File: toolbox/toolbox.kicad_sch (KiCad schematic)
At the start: 0 parts

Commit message: added logic shifting
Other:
- removed sheet circuit-proctection
- added sheet logic-shifting (logic-shifting.kicad_sch)
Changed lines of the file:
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@@
 (kicad_sch (version 20211123) (generator eeschema)
   (paper "A4")
-  (sheet (at 45.72 73.66) (size 41.91 20.32) (fields_autoplaced)
+  (sheet (at 46.99 38.1) (size 45.72 17.78) (fields_autoplaced)
     (stroke (width 0.1524) (type solid) (color 0 0 0 0))
     (fill (color 0 0 0 0.0000))
-    (property "Sheet name" "circuit-proctection" (id 0) (at 45.72 72.9484 0)
+    (property "Sheet name" "LED-indicators" (id 0) (at 46.99 37.3884 0)
       (effects (font (size 1.27 1.27)) (justify left bottom))
     )
-    (property "Sheet file" "circuit-proctection.kicad_sch" (id 1) (at 45.72 94.5646 0)
+    (property "Sheet file" "untitled.kicad_sch" (id 1) (at 46.99 56.4646 0)
       (effects (font (size 1.27 1.27)) (justify left top))
     )
   )
-  (sheet (at 39.37 38.1) (size 45.72 17.78) (fields_autoplaced)
+  (sheet (at 46.99 66.04) (size 45.72 17.78) (fields_autoplaced)
     (stroke (width 0.1524) (type solid) (color 0 0 0 0))
     (fill (color 0 0 0 0.0000))
-    (property "Sheet name" "LED-indicators" (id 0) (at 39.37 37.3884 0)
+    (property "Sheet name" "logic-shifting" (id 0) (at 46.99 65.3284 0)
       (effects (font (size 1.27 1.27)) (justify left bottom))
     )
-    (property "Sheet file" "untitled.kicad_sch" (id 1) (at 39.37 56.4646 0)
+    (property "Sheet file" "logic-shifting.kicad_sch" (id 1) (at 46.99 84.4046 0)
       (effects (font (size 1.27 1.27)) (justify left top))
     )
@@
     (path "/" (page "1"))
     (path "/1b2afd57-d1a0-4fee-a173-2bd4ec4407d2" (page "2"))
-    (path "/0ef72fb1-9a74-4a61-8ab7-5a4a580b8ed0" (page "3"))
+    (path "/2eae8836-7aeb-411d-86a3-74045163b3dc" (page "3"))
   )
   (symbol_instances
-    (path "/1b2afd57-d1a0-4fee-a173-2bd4ec4407d2/6bc2a5b6-23b9-4465-86f6-cf66a0e9698e"
-      (reference "#PWR?") (unit 1) (value "GND1") (footprint "")
-    )
     (path "/1b2afd57-d1a0-4fee-a173-2bd4ec4407d2/8a5ff09f-7252-4a5d-bcb9-7621274b5a31"
-      (reference "#PWR?") (unit 1) (value "+12V") (footprint "")
+      (reference "#PWR01") (unit 1) (value "+12V") (footprint "")
     )
     (path "/1b2afd57-d1a0-4fee-a173-2bd4ec4407d2/ac0bf3aa-43ac-4807-9671-687abc4cb1db"
-      (reference "#PWR?") (unit 1) (value "GND1") (footprint "")
+      (reference "#PWR02") (unit 1) (value "GND1") (footprint "")
+    )
+    (path "/1b2afd57-d1a0-4fee-a173-2bd4ec4407d2/d631fecf-1e8a-41e4-b2c3-fff52c91425c"
+      (reference "#PWR03") (unit 1) (value "+12V") (footprint "")
+    )
+    (path "/1b2afd57-d1a0-4fee-a173-2bd4ec4407d2/6bc2a5b6-23b9-4465-86f6-cf66a0e9698e"
+      (reference "#PWR04") (unit 1) (value "GND1") (footprint "")
     )
     (path "/1b2afd57-d1a0-4fee-a173-2bd4ec4407d2/b213f021-1a63-46c5-adbc-2b9ab0b5658d"
-      (reference "#PWR?") (unit 1) (value "GND1") (footprint "")
+      (reference "#PWR05") (unit 1) (value "GND1") (footprint "")
     )
-    (path "/1b2afd57-d1a0-4fee-a173-2bd4ec4407d2/d631fecf-1e8a-41e4-b2c3-fff52c91425c"
-      (reference "#PWR?") (unit 1) (value "+12V") (footprint "")
+    (path "/2eae8836-7aeb-411d-86a3-74045163b3dc/49f7c971-dd53-4f55-84d8-29bb418d08d9"
+      (reference "#PWR06") (unit 1) (value "+3.3V") (footprint "")
+    )
+    (path "/2eae8836-7aeb-411d-86a3-74045163b3dc/a614248d-ea71-4c4c-adfa-7e57746c2e4a"
+      (reference "#PWR07") (unit 1) (value "+3.3V") (footprint "")
+    )
+    (path "/2eae8836-7aeb-411d-86a3-74045163b3dc/bfa6977f-bce4-4d70-a34c-574b7db849b5"
+      (reference "#PWR08") (unit 1) (value "+5V") (footprint "")
     )
     (path "/1b2afd57-d1a0-4fee-a173-2bd4ec4407d2/62b47200-86fd-47e9-89ee-41885bec3973"
-      (reference "D?") (unit 1) (value "LED") (footprint "")
+      (reference "D1") (unit 1) (value "LED") (footprint "")
     )
     (path "/1b2afd57-d1a0-4fee-a173-2bd4ec4407d2/f5519cb4-891a-4d44-bcf5-214752117d34"
-      (reference "D?") (unit 1) (value "LED_Dual_Bidirectional") (footprint "")
+      (reference "D2") (unit 1) (value "LED_Dual_Bidirectional") (footprint "")
     )
     (path "/1b2afd57-d1a0-4fee-a173-2bd4ec4407d2/358dc423-8799-47ea-b50e-cd8d3f59a56b"
-      (reference "Q?") (unit 1) (value "2N3904") (footprint "Package_TO_SOT_THT:TO-92_Inline")
+      (reference "Q1") (unit 1) (value "2N3904") (footprint "Package_TO_SOT_THT:TO-92_Inline")
     )
     (path "/1b2afd57-d1a0-4fee-a173-2bd4ec4407d2/3c467d87-e7e4-4506-a99e-a2e098c9955e"
-      (reference "Q?") (unit 1) (value "2N3904") (footprint "Package_TO_SOT_THT:TO-92_Inline")
+      (reference "Q2") (unit 1) (value "2N3904") (footprint "Package_TO_SOT_THT:TO-92_Inline")
+    )
+    (path "/2eae8836-7aeb-411d-86a3-74045163b3dc/b40c593d-d1c8-415d-8cfc-92d3d461d45e"
+      (reference "Q3") (unit 1) (value "IRLZ44N") (footprint "Package_TO_SOT_THT:TO-220-3_Vertical")
+    )
+    (path "/1b2afd57-d1a0-4fee-a173-2bd4ec4407d2/ad975569-5dc9-4ab5-a34f-936371926baf"
+      (reference "R1") (unit 1) (value "R_US") (footprint "")
+    )
+    (path "/1b2afd57-d1a0-4fee-a173-2bd4ec4407d2/a57405f9-fd2f-49b0-8c2c-6f78ee93dfce"
+      (reference "R2") (unit 1) (value "560") (footprint "")
     )
     (path "/1b2afd57-d1a0-4fee-a173-2bd4ec4407d2/71ce2297-3bb4-4e32-aa63-b251ac894308"
-      (reference "R?") (unit 1) (value "560") (footprint "")
+      (reference "R3") (unit 1) (value "560") (footprint "")
+    )
+    (path "/1b2afd57-d1a0-4fee-a173-2bd4ec4407d2/ad86b028-df16-41eb-9f9c-520f29100440"
+      (reference "R4") (unit 1) (value "56k") (footprint "")
     )
     (path "/1b2afd57-d1a0-4fee-a173-2bd4ec4407d2/864b8362-7e0a-47c0-9bfd-7184da1c3abf"
-      (reference "R?") (unit 1) (value "68k") (footprint "")
+      (reference "R5") (unit 1) (value "68k") (footprint "")
     )
-    (path "/1b2afd57-d1a0-4fee-a173-2bd4ec4407d2/a57405f9-fd2f-49b0-8c2c-6f78ee93dfce"
-      (reference "R?") (unit 1) (value "560") (footprint "")
+    (path "/2eae8836-7aeb-411d-86a3-74045163b3dc/6afee0e1-2b7b-4739-87e8-3e8ed3b1bbe5"
+      (reference "R6") (unit 1) (value "10k") (footprint "")
     )
-    (path "/1b2afd57-d1a0-4fee-a173-2bd4ec4407d2/ad86b028-df16-41eb-9f9c-520f29100440"
-      (reference "R?") (unit 1) (value "56k") (footprint "")
-    )
-    (path "/1b2afd57-d1a0-4fee-a173-2bd4ec4407d2/ad975569-5dc9-4ab5-a34f-936371926baf"
-      (reference "R?") (unit 1) (value "R_US") (footprint "")
+    (path "/2eae8836-7aeb-411d-86a3-74045163b3dc/5349268a-ca0b-4e21-86db-1f2a615e78e6"
+      (reference "R7") (unit 1) (value "1Ok") (footprint "")
     )
     (path "/1b2afd57-d1a0-4fee-a173-2bd4ec4407d2/983e6fc9-c213-4d14-9fb0-8b9741c349b1"
-      (reference "SW?") (unit 1) (value "SW_SPST") (footprint "")
+      (reference "SW1") (unit 1) (value "SW_SPST") (footprint "")
     )
   )

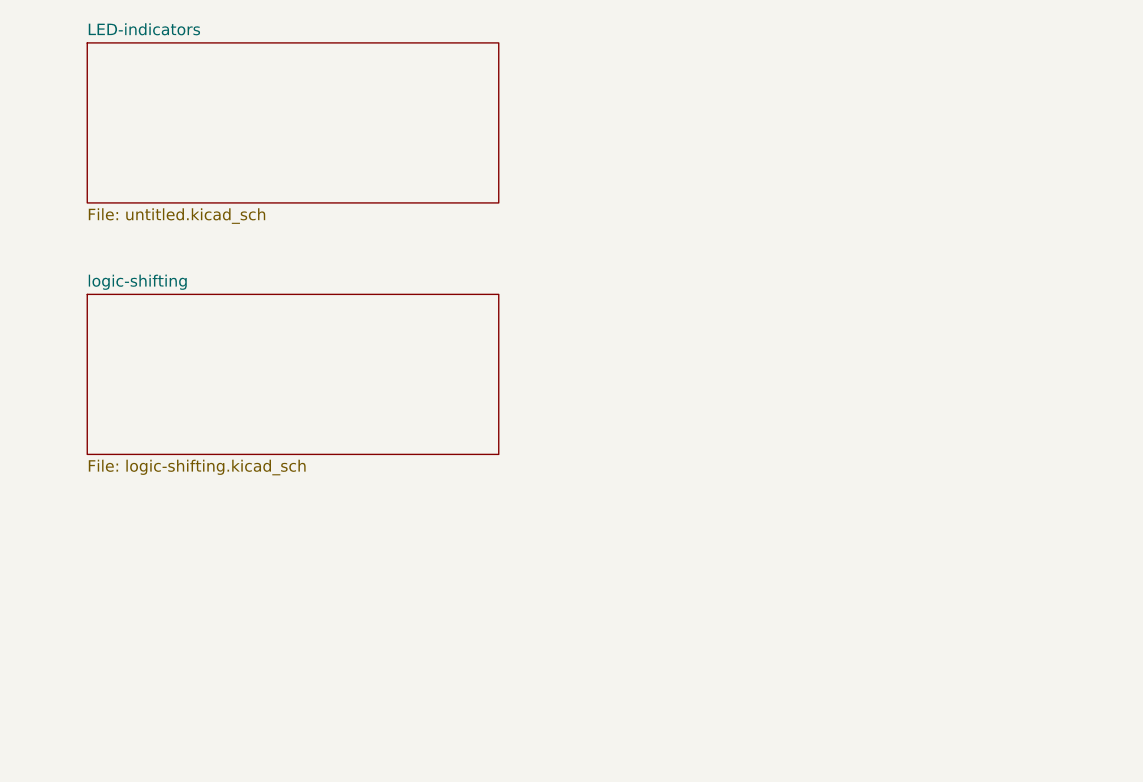
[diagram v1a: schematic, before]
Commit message: added io extension
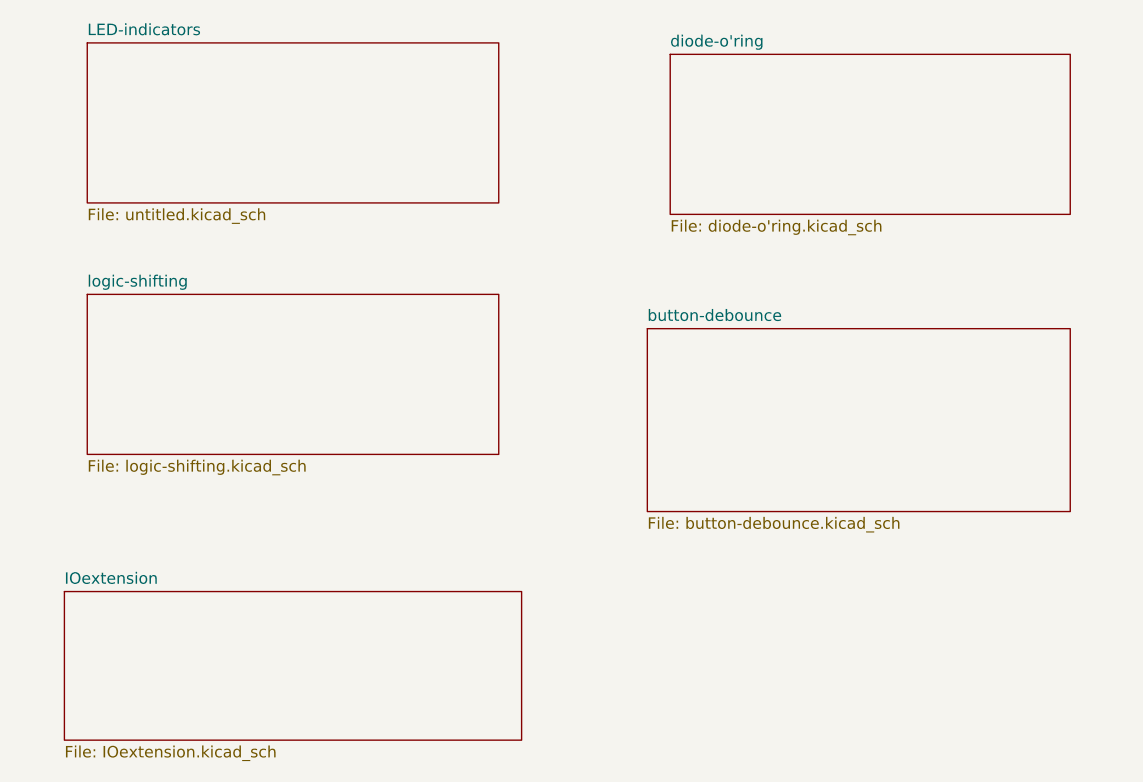
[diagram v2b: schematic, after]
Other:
- added sheet IOextension (IOextension.kicad_sch)
- added sheet button-debounce (button-debounce.kicad_sch)
- added sheet diode-o'ring (diode-o'ring.kicad_sch)

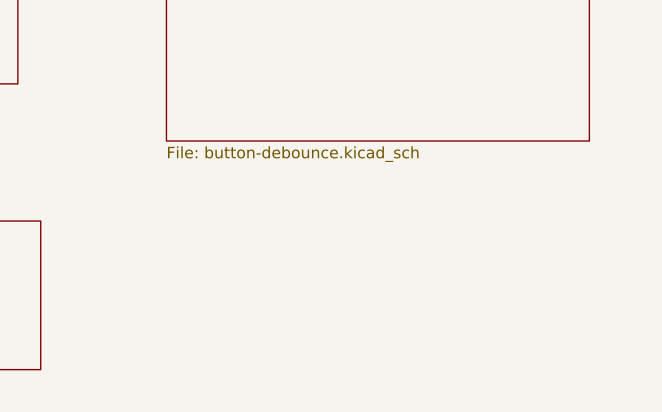
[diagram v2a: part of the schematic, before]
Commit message: added p-mosfet prcotection circuit
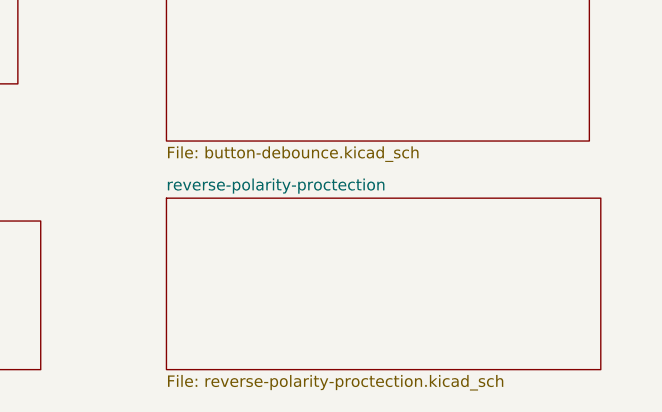
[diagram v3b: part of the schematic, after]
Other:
- added sheet reverse-polarity-proctection (reverse-polarity-proctection.kicad_sch)
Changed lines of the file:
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@@
+    )
+  )
+  (sheet (at 109.22 96.52) (size 48.26 19.05) (fields_autoplaced)
+    (stroke (width 0.1524) (type solid) (color 0 0 0 0))
+    (fill (color 0 0 0 0.0000))
+    (property "Sheet name" "reverse-polarity-proctection" (id 0) (at 109.22 95.8084 0)
+      (effects (font (size 1.27 1.27)) (justify left bottom))
+    )
+    (property "Sheet file" "reverse-polarity-proctection.kicad_sch" (id 1) (at 109.22 116.1546 0)
+      (effects (font (size 1.27 1.27)) (justify left top))
     )
   )
@@
     (path "/02027032-558b-4aa6-9b5b-d65226f679db" (page "5"))
     (path "/91bca55d-a420-4f35-a541-acc4964088cf" (page "6"))
+    (path "/574670bc-b2c5-46ec-8c41-c545a47f0816" (page "7"))
   )
   (symbol_instances
@@
       (reference "#PWR021") (unit 1) (value "GND1") (footprint "")
     )
+    (path "/91bca55d-a420-4f35-a541-acc4964088cf/c6332154-b60a-41f6-a67b-88ec3c67ae2d"
+      (reference "#PWR022") (unit 1) (value "VCC") (footprint "")
+    )
+    (path "/91bca55d-a420-4f35-a541-acc4964088cf/8b6f76e2-930d-4d66-bfe0-9f18ad1b58a9"
+      (reference "#PWR023") (unit 1) (value "GND1") (footprint "")
+    )
+    (path "/91bca55d-a420-4f35-a541-acc4964088cf/a9792ada-0920-49eb-a543-a36cf69ccd84"
+      (reference "#PWR024") (unit 1) (value "GND1") (footprint "")
+    )
+    (path "/91bca55d-a420-4f35-a541-acc4964088cf/642f2c2b-6bdf-4666-a16b-72f80e133292"
+      (reference "#PWR025") (unit 1) (value "GND1") (footprint "")
+    )
+    (path "/91bca55d-a420-4f35-a541-acc4964088cf/6a8dd1b7-5cb7-456e-b5b8-c08da6be2e47"
+      (reference "#PWR026") (unit 1) (value "GND1") (footprint "")
+    )
     (path "/91bca55d-a420-4f35-a541-acc4964088cf/16fc6da5-cd06-4073-9c3b-e67e75cd58a1"
-      (reference "#PWR?") (unit 1) (value "GND1") (footprint "")
+      (reference "#PWR027") (unit 1) (value "GND1") (footprint "")
     )
     (path "/91bca55d-a420-4f35-a541-acc4964088cf/48aade0b-7410-49d7-b71a-aac83b0b477b"
-      (reference "#PWR?") (unit 1) (value "GND1") (footprint "")
-    )
-    (path "/91bca55d-a420-4f35-a541-acc4964088cf/642f2c2b-6bdf-4666-a16b-72f80e133292"
-      (reference "#PWR?") (unit 1) (value "GND1") (footprint "")
-    )
-    (path "/91bca55d-a420-4f35-a541-acc4964088cf/6a8dd1b7-5cb7-456e-b5b8-c08da6be2e47"
-      (reference "#PWR?") (unit 1) (value "GND1") (footprint "")
+      (reference "#PWR028") (unit 1) (value "GND1") (footprint "")
     )
     (path "/91bca55d-a420-4f35-a541-acc4964088cf/7abbe852-1d8f-4067-aaba-30b9d7a5d6ce"
-      (reference "#PWR?") (unit 1) (value "GND1") (footprint "")
-    )
-    (path "/91bca55d-a420-4f35-a541-acc4964088cf/8b6f76e2-930d-4d66-bfe0-9f18ad1b58a9"
-      (reference "#PWR?") (unit 1) (value "GND1") (footprint "")
-    )
-    (path "/91bca55d-a420-4f35-a541-acc4964088cf/a9792ada-0920-49eb-a543-a36cf69ccd84"
-      (reference "#PWR?") (unit 1) (value "GND1") (footprint "")
+      (reference "#PWR029") (unit 1) (value "GND1") (footprint "")
     )
     (path "/91bca55d-a420-4f35-a541-acc4964088cf/be496dee-22a6-4dc3-aa84-f033d9c1c61f"
-      (reference "#PWR?") (unit 1) (value "GND1") (footprint "")
-    )
-    (path "/91bca55d-a420-4f35-a541-acc4964088cf/c6332154-b60a-41f6-a67b-88ec3c67ae2d"
-      (reference "#PWR?") (unit 1) (value "VCC") (footprint "")
+      (reference "#PWR030") (unit 1) (value "GND1") (footprint "")
     )
     (path "/91bca55d-a420-4f35-a541-acc4964088cf/f0124583-3c8e-4cde-b218-e4193e2a98b0"
-      (reference "#PWR?") (unit 1) (value "GND1") (footprint "")
+      (reference "#PWR031") (unit 1) (value "GND1") (footprint "")
     )
     (path "/9c7d5fec-3027-49e1-988d-2ce44d9421c2/5d8dbb9f-dccc-46a9-9565-eb17784777c8"
@@
     )
     (path "/91bca55d-a420-4f35-a541-acc4964088cf/027d924e-bfb6-4d68-bd82-a449d1b64387"
-      (reference "D?") (unit 1) (value "LED") (footprint "")
+      (reference "D6") (unit 1) (value "LED") (footprint "")
+    )
+    (path "/91bca55d-a420-4f35-a541-acc4964088cf/99459ba0-2496-4a8b-ba06-7a8f42f3faa9"
+      (reference "D7") (unit 1) (value "LED") (footprint "")
     )
     (path "/91bca55d-a420-4f35-a541-acc4964088cf/098605c0-cbc5-4648-80e1-356ff2a203de"
-      (reference "D?") (unit 1) (value "LED") (footprint "")
+      (reference "D8") (unit 1) (value "LED") (footprint "")
     )
     (path "/91bca55d-a420-4f35-a541-acc4964088cf/1d5d690a-e719-4d2e-9459-d63a813f704a"
-      (reference "D?") (unit 1) (value "LED") (footprint "")
+      (reference "D9") (unit 1) (value "LED") (footprint "")
+    )
+    (path "/91bca55d-a420-4f35-a541-acc4964088cf/af6c626d-801f-492e-b077-aaa46cdfd745"
+      (reference "D10") (unit 1) (value "LED") (footprint "")
     )
     (path "/91bca55d-a420-4f35-a541-acc4964088cf/78ca4b48-886a-4993-84f7-48dc022017ae"
-      (reference "D?") (unit 1) (value "LED") (footprint "")
+      (reference "D11") (unit 1) (value "LED") (footprint "")
     )
     (path "/91bca55d-a420-4f35-a541-acc4964088cf/7c6ea85d-8ec4-41c6-8b90-8038dfa112e7"
-      (reference "D?") (unit 1) (value "LED") (footprint "")
+      (reference "D12") (unit 1) (value "LED") (footprint "")
+    )
+    (path "/91bca55d-a420-4f35-a541-acc4964088cf/8f1340b3-928c-4cc5-a021-5695b97fae68"
+      (reference "D13") (unit 1) (value "LED") (footprint "")
     )
     (path "/91bca55d-a420-4f35-a541-acc4964088cf/85cf439f-8dff-43c3-9f6e-dcdd8abdfa06"
-      (reference "D?") (unit 1) (value "LED") (footprint "")
-    )
-    (path "/91bca55d-a420-4f35-a541-acc4964088cf/8f1340b3-928c-4cc5-a021-5695b97fae68"
-      (reference "D?") (unit 1) (value "LED") (footprint "")
-    )
-    (path "/91bca55d-a420-4f35-a541-acc4964088cf/99459ba0-2496-4a8b-ba06-7a8f42f3faa9"
-      (reference "D?") (unit 1) (value "LED") (footprint "")
-    )
-    (path "/91bca55d-a420-4f35-a541-acc4964088cf/af6c626d-801f-492e-b077-aaa46cdfd745"
-      (reference "D?") (unit 1) (value "LED") (footprint "")
+      (reference "D14") (unit 1) (value "LED") (footprint "")
+    )
+    (path "/574670bc-b2c5-46ec-8c41-c545a47f0816/54f2ed64-7dec-4129-91f7-e8af9e613836"
+      (reference "D15") (unit 1) (value "D_Zener") (footprint "")
     )
     (path "/9c7d5fec-3027-49e1-988d-2ce44d9421c2/7860bc77-f4b3-442d-b59f-77de8851ff2c"
@@
       (reference "Q4") (unit 1) (value "DMG2301L") (footprint "Package_TO_SOT_SMD:SOT-23")
     )
+    (path "/574670bc-b2c5-46ec-8c41-c545a47f0816/15bb0b6e-e8bf-4593-9a10-1c1ce942dfaf"
+      (reference "Q5") (unit 1) (value "IRLML6401") (footprint "Package_TO_SOT_SMD:SOT-23")
+    )
     (path "/1b2afd57-d1a0-4fee-a173-2bd4ec4407d2/ad975569-5dc9-4ab5-a34f-936371926baf"
       (reference "R1") (unit 1) (value "R_US") (footprint "")
@@
       (reference "R11") (unit 1) (value "10k") (footprint "")
     )
+    (path "/91bca55d-a420-4f35-a541-acc4964088cf/3e361bd9-b4ad-4250-ad5b-187253e1363d"
+      (reference "R12") (unit 1) (value "220") (footprint "")
+    )
+    (path "/91bca55d-a420-4f35-a541-acc4964088cf/793b9097-5436-40e5-bace-4c1740d8a64c"
+      (reference "R13") (unit 1) (value "220") (footprint "")
+    )
+    (path "/91bca55d-a420-4f35-a541-acc4964088cf/bcf729e5-5112-43eb-be07-fe24ba8636d2"
+      (reference "R14") (unit 1) (value "220") (footprint "")
+    )
     (path "/91bca55d-a420-4f35-a541-acc4964088cf/164f13a8-13df-4f3d-9dd4-7bb61d609937"
-      (reference "R?") (unit 1) (value "220") (footprint "")
+      (reference "R15") (unit 1) (value "220") (footprint "")
+    )
+    (path "/91bca55d-a420-4f35-a541-acc4964088cf/5fa22f6c-516d-475e-b68a-2a1dc104ad5f"
+      (reference "R16") (unit 1) (value "220") (footprint "")
+    )
+    (path "/91bca55d-a420-4f35-a541-acc4964088cf/4c85bf25-e488-4ee9-8f42-3b0eeccf9feb"
+      (reference "R17") (unit 1) (value "220") (footprint "")
+    )
+    (path "/91bca55d-a420-4f35-a541-acc4964088cf/f69ba61f-50b2-47f7-a98e-39ae6062226d"
+      (reference "R18") (unit 1) (value "220") (footprint "")
+    )
+    (path "/91bca55d-a420-4f35-a541-acc4964088cf/abdd08b5-7b4b-44b7-b845-1cb447f69ae7"
+      (reference "R19") (unit 1) (value "220") (footprint "")
     )
     (path "/91bca55d-a420-4f35-a541-acc4964088cf/3604f829-edb1-43b2-a0c5-bc88a2d00b64"
-      (reference "R?") (unit 1) (value "220") (footprint "")
-    )
-    (path "/91bca55d-a420-4f35-a541-acc4964088cf/3e361bd9-b4ad-4250-ad5b-187253e1363d"
-      (reference "R?") (unit 1) (value "220") (footprint "")
-    )
-    (path "/91bca55d-a420-4f35-a541-acc4964088cf/4c85bf25-e488-4ee9-8f42-3b0eeccf9feb"
-      (reference "R?") (unit 1) (value "220") (footprint "")
-    )
-    (path "/91bca55d-a420-4f35-a541-acc4964088cf/5fa22f6c-516d-475e-b68a-2a1dc104ad5f"
-      (reference "R?") (unit 1) (value "220") (footprint "")
-    )
-    (path "/91bca55d-a420-4f35-a541-acc4964088cf/793b9097-5436-40e5-bace-4c1740d8a64c"
-      (reference "R?") (unit 1) (value "220") (footprint "")
-    )
-    (path "/91bca55d-a420-4f35-a541-acc4964088cf/abdd08b5-7b4b-44b7-b845-1cb447f69ae7"
-      (reference "R?") (unit 1) (value "220") (footprint "")
-    )
-    (path "/91bca55d-a420-4f35-a541-acc4964088cf/bcf729e5-5112-43eb-be07-fe24ba8636d2"
-      (reference "R?") (unit 1) (value "220") (footprint "")
-    )
-    (path "/91bca55d-a420-4f35-a541-acc4964088cf/f69ba61f-50b2-47f7-a98e-39ae6062226d"
-      (reference "R?") (unit 1) (value "220") (footprint "")
+      (reference "R20") (unit 1) (value "220") (footprint "")
+    )
+    (path "/574670bc-b2c5-46ec-8c41-c545a47f0816/d95391fc-cfe8-4f75-b13f-053e2dd73c84"
+      (reference "R21") (unit 1) (value "R_US") (footprint "")
     )
     (path "/1b2afd57-d1a0-4fee-a173-2bd4ec4407d2/983e6fc9-c213-4d14-9fb0-8b9741c349b1"
@@
     )
     (path "/91bca55d-a420-4f35-a541-acc4964088cf/16a06a7e-d254-4a9c-a302-c51bdb0a1550"
-      (reference "U?") (unit 1) (value "74HC595") (footprint "")
-    )
-  )
+      (reference "U4") (unit 1) (value "74HC595") (footprint "")
+    )
+  )
